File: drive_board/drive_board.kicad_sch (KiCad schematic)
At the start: 7 parts, among them J2 RJ45_LED_Shielded

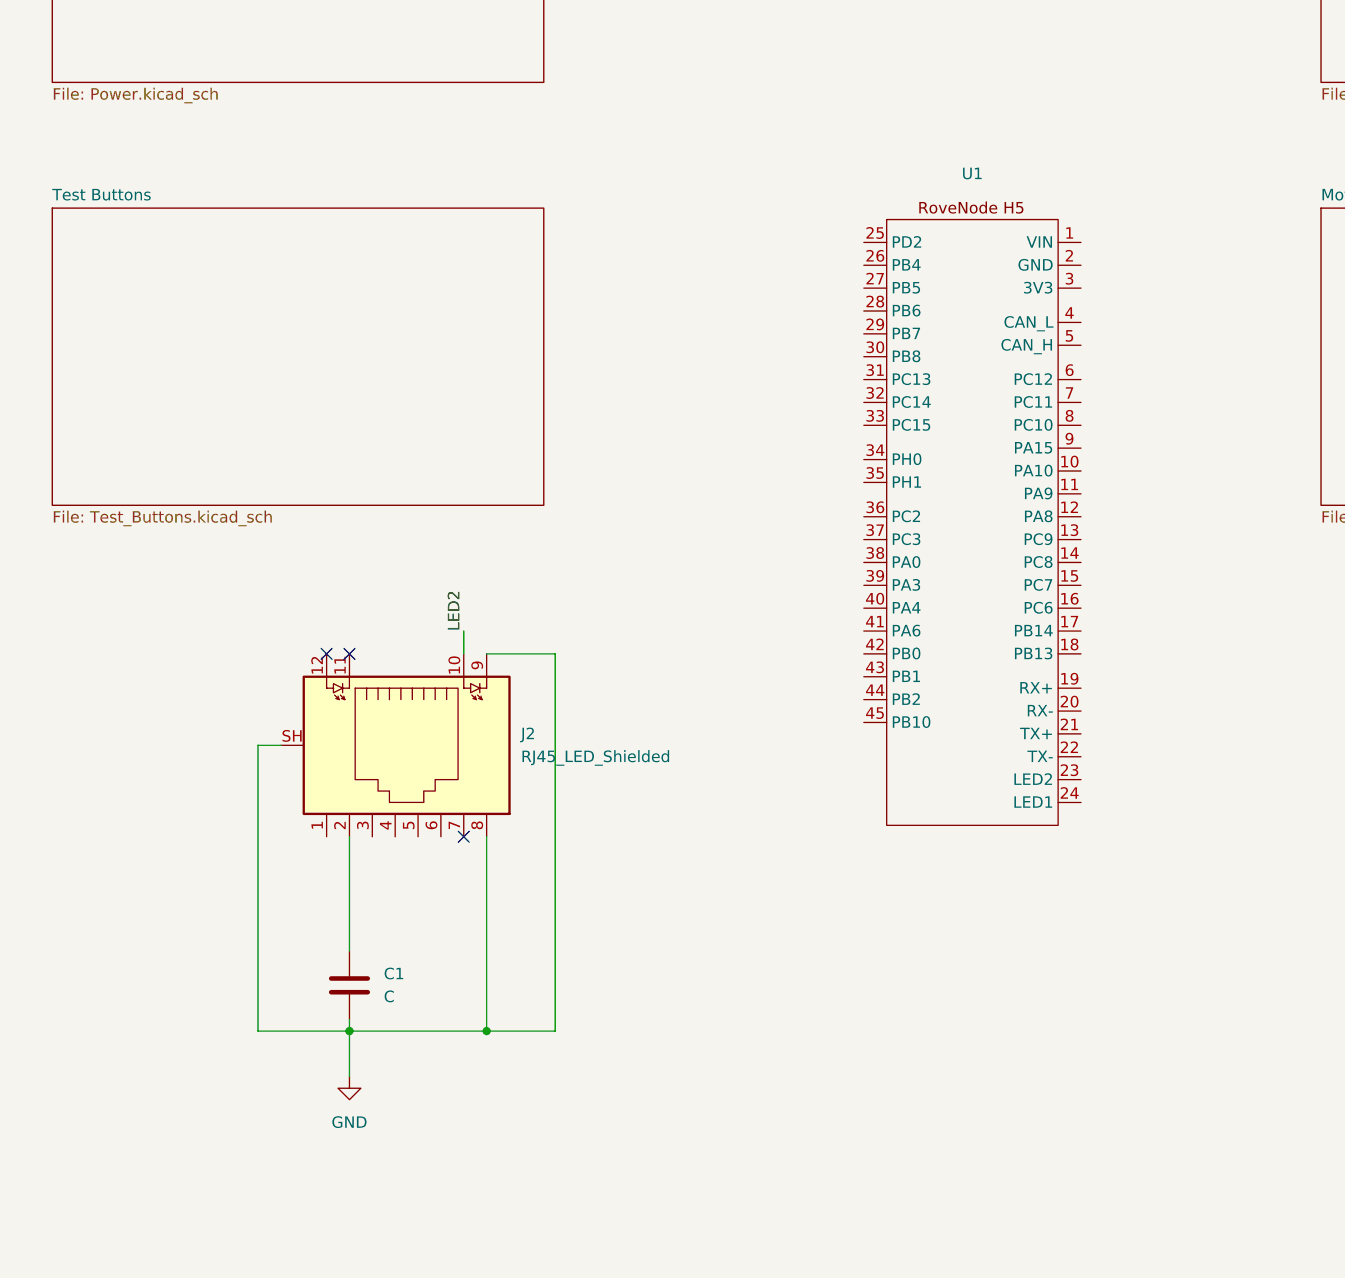
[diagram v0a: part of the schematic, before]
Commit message: New Stuff
- Reverse voltage protection
- D-Pad for test buttons
- Rotary encoder for test buttons
- Finished ethernet circuit
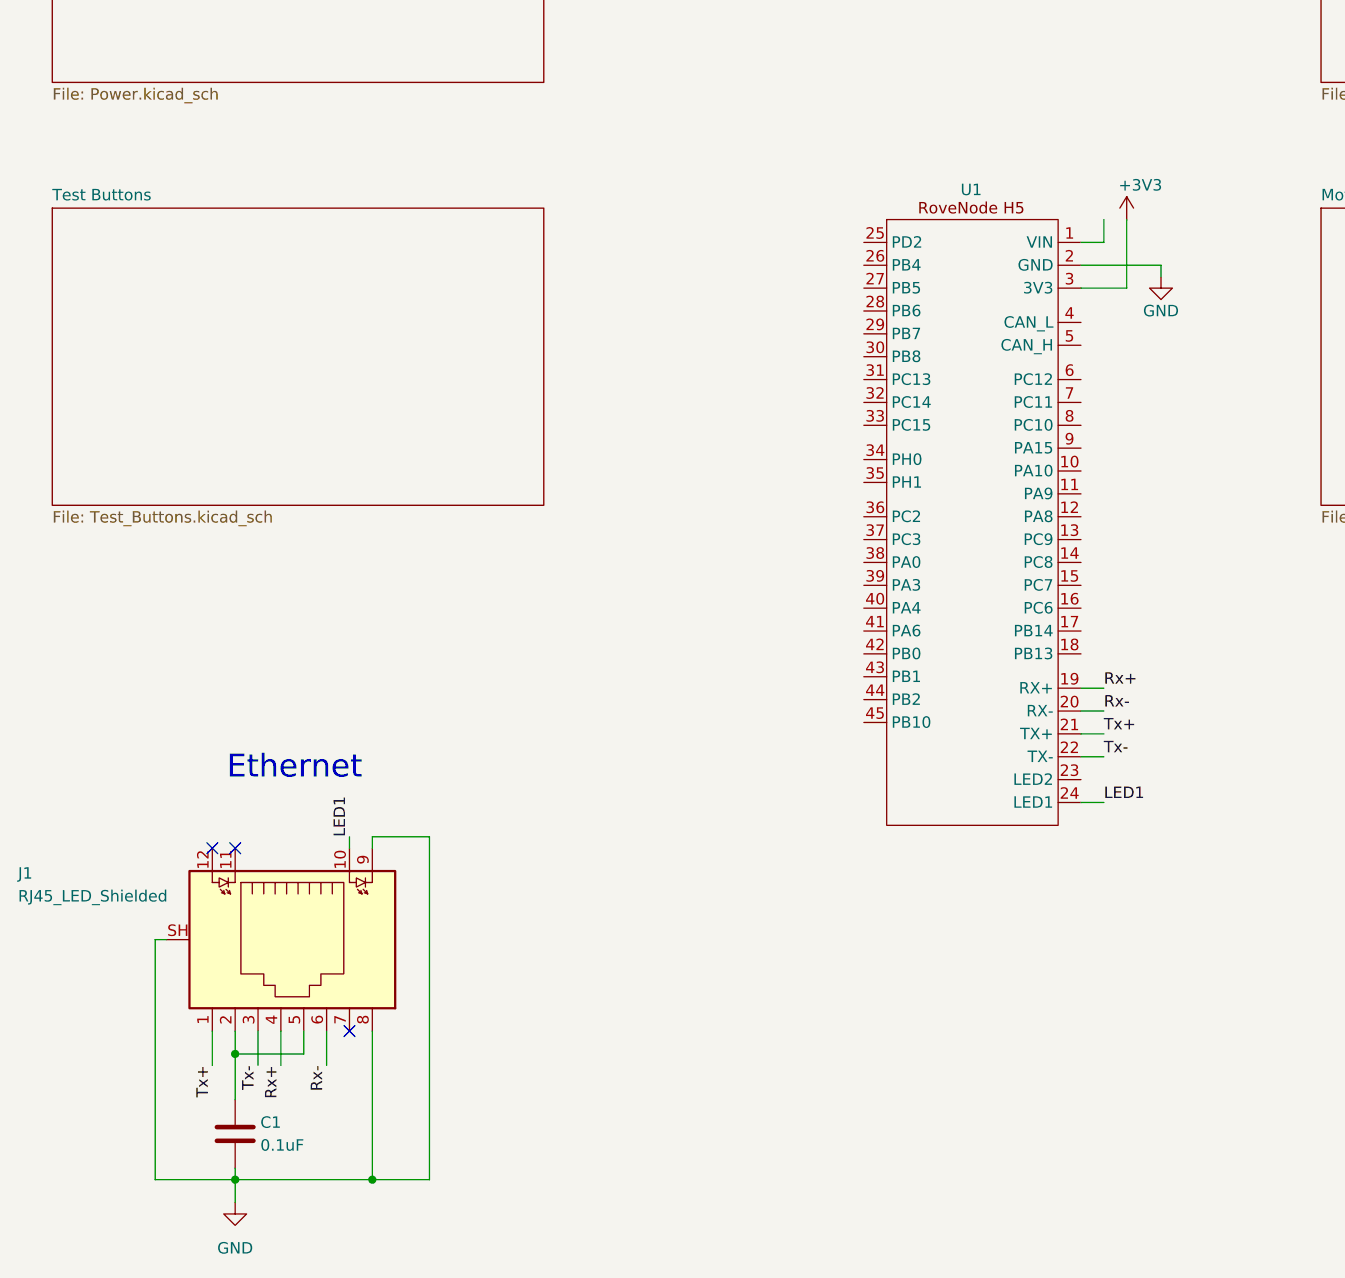
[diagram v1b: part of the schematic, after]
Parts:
- C1: value C -> 0.1uF
- renumbered J2 to J1
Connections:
- net LED2 is gone; now on net LED1: J1.10
- net GND: now also U1.2 (GND)
- net Rx+: now reaches U1.19 (RX+)
- net Rx+: now also J1.4
- net Rx-: now reaches U1.20 (RX-)
- net Rx-: now also J1.6
- net Tx+: now reaches U1.21 (TX+)
- net Tx+: now also J1.1
- net Tx-: now reaches U1.22 (TX-)
- net Tx-: now also J1.3
- net LED1: now reaches U1.24 (LED1)
- net +3V3: now reaches U1.3 (3V3)
- net at C1.1, J1.2: now also J1.5
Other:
- note added: "Ethernet"
- moved on the sheet: C1, J1

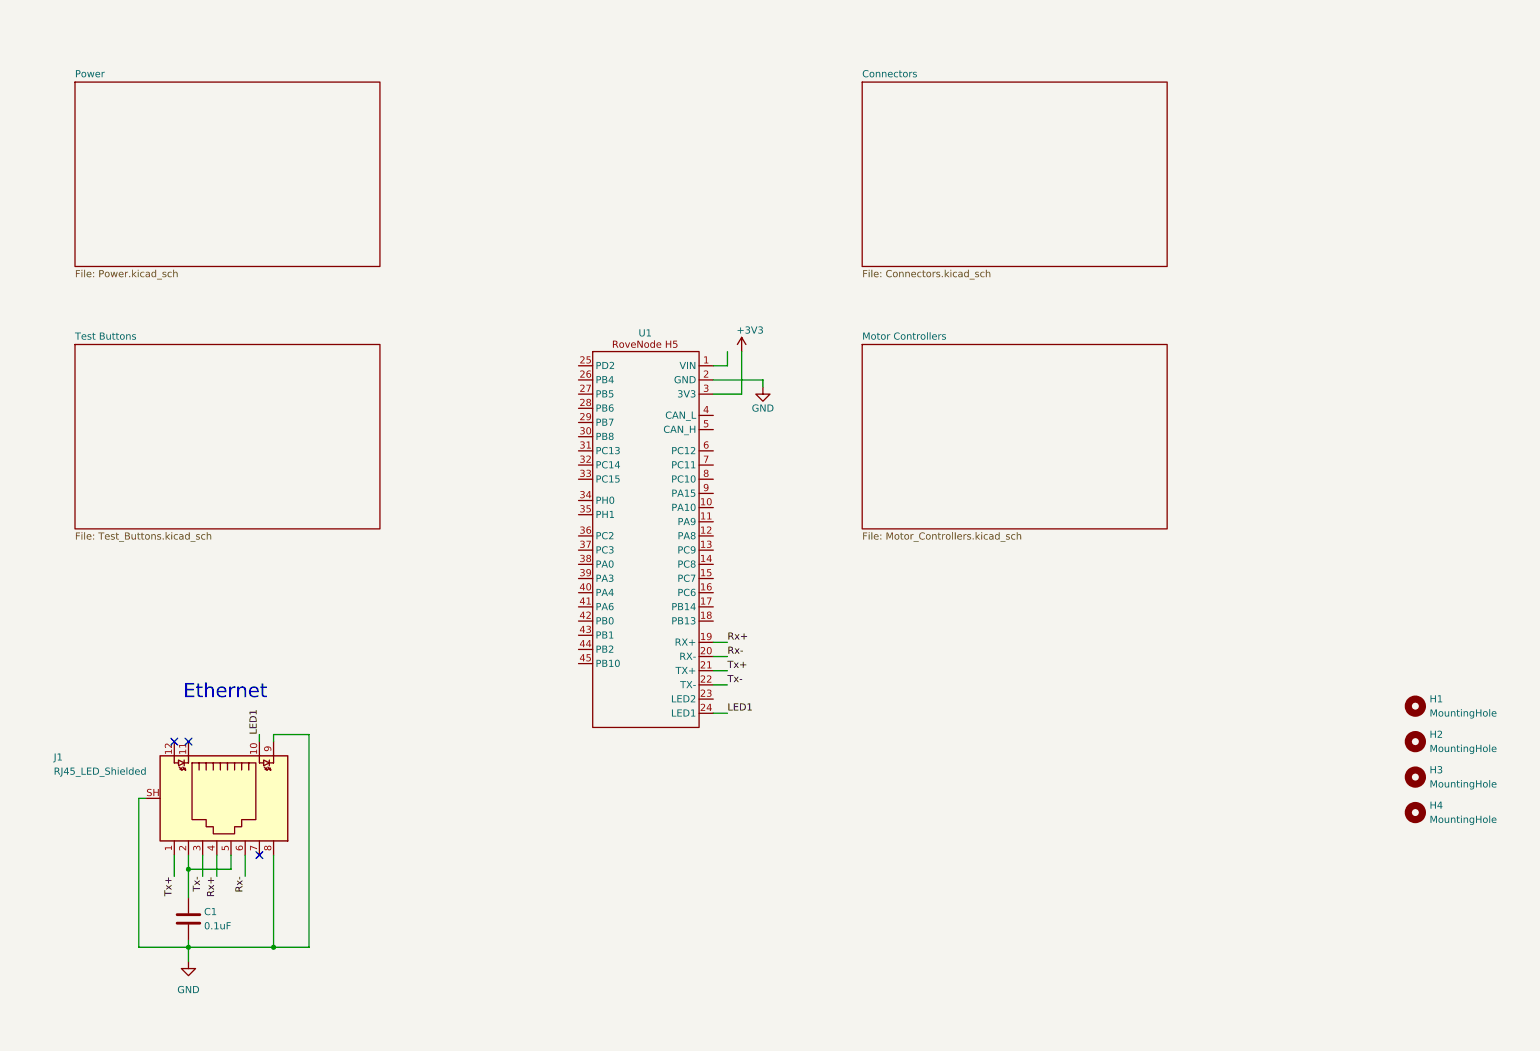
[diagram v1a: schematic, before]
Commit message: More New Stuff
- Assigned pins on RoveNode
- Added some connectors
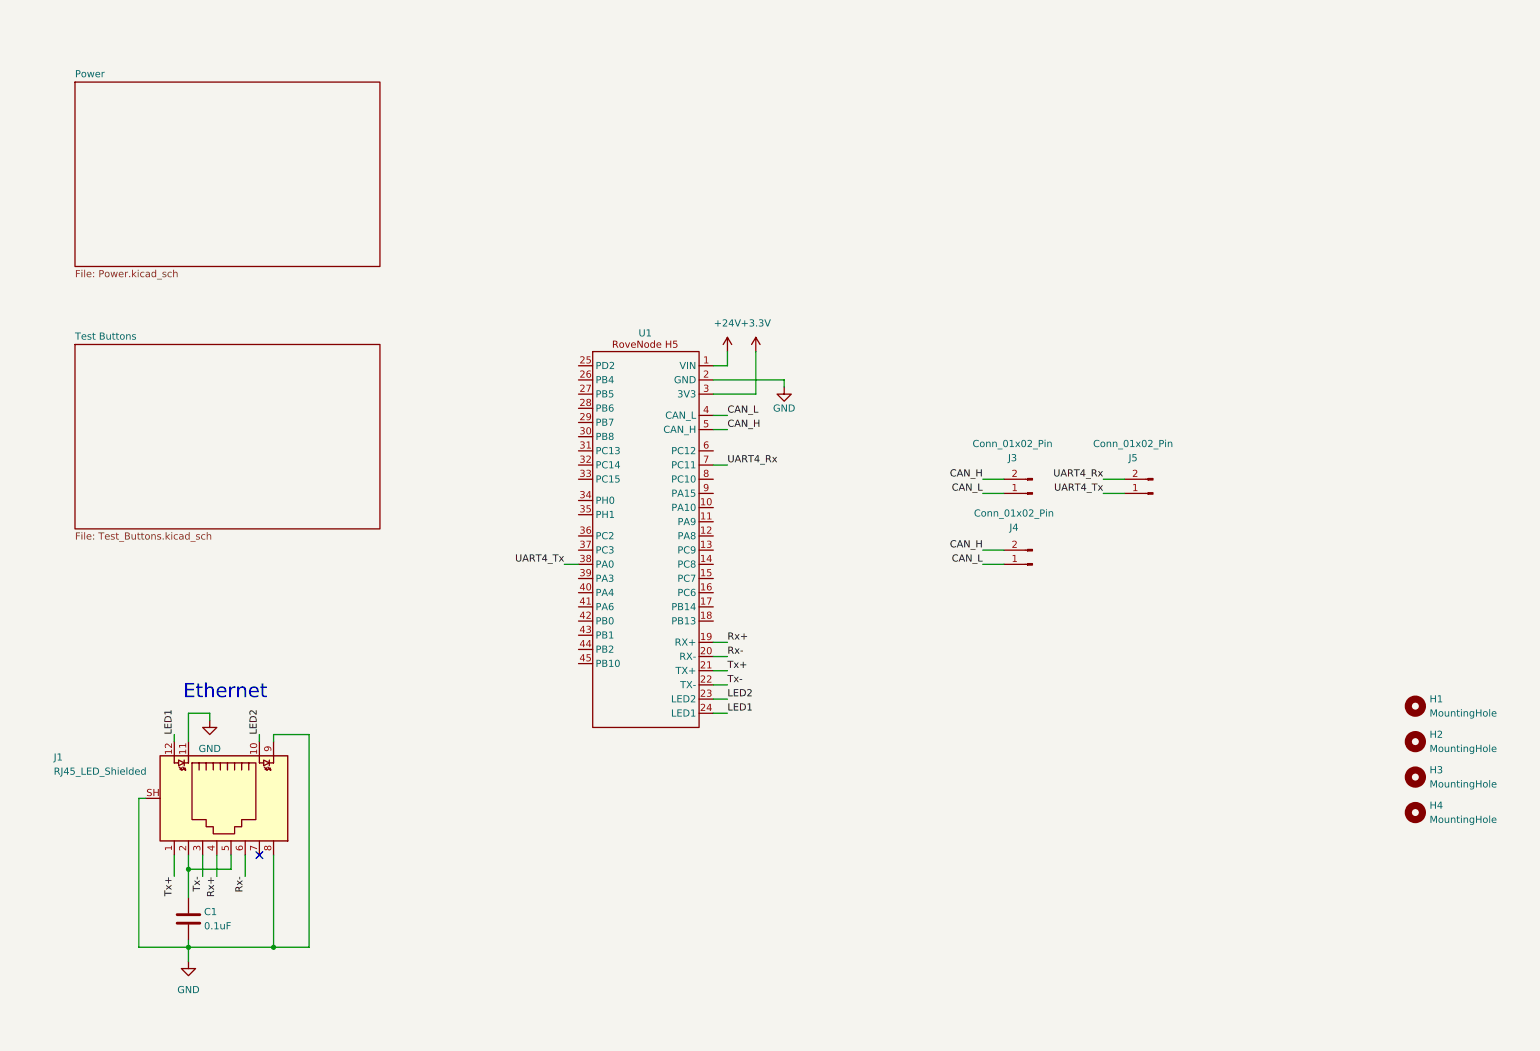
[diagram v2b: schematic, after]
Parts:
- added J3, J4, J5: Conn_01x02_Pin, Package_DFN_QFN:QFN-20-1EP_5x5mm_P0.65mm_EP3.35x3.35mm, symbol Connector:Conn_01x02_Pin
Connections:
- net GND: now also J1.11
- net LED1: now also J1.12; no longer J1.10
- net +24V: now reaches U1.1 (VIN)
- net LED2: now reaches U1.23 (LED2)
- net LED2: now also J1.10
- net UART4_Tx: now reaches U1.38 (PA0)
- net UART4_Tx: now also J5.1 (Pin_1)
- net CAN_L: now reaches U1.4 (CAN_L)
- net CAN_L: now also J3.1 (Pin_1), J4.1 (Pin_1)
- net CAN_H: now reaches U1.5 (CAN_H)
- net CAN_H: now also J3.2 (Pin_2), J4.2 (Pin_2)
- net UART4_Rx: now reaches U1.7 (PC11)
- net UART4_Rx: now also J5.2 (Pin_2)
- net +3V3 renamed +3.3V
- no-connect marks 3 -> 1
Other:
- removed sheet Connectors
- removed sheet Motor Controllers

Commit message: Even More New Stuff
- CAN Transceiver
- Global and hierarchal labels
- How the heck does the rotary encoder work? Lmk when I'm in the office.
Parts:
- added R9: 120, Resistor_SMD:R_0603_1608Metric_Pad0.98x0.95mm_HandSolder, symbol Device:R_US
- added U3: SN65HVD232, Package_SO:SOIC-8_3.9x4.9mm_P1.27mm, symbol Interface_CAN_LIN:SN65HVD232
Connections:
- net GND: now also U3.2 (GND)
- net CAN2_TX: now reaches U1.18 (PB13)
- net CAN2_RX: now reaches U1.27 (PB5)
- net CAN2_RX: now also U3.4 (R)
- net CAN_H renamed CAN_H_1
- net CAN_H_1: no longer J4.2 (Pin_2)
- net CAN_L renamed CAN_L_1
- net CAN_L_1: no longer J4.1 (Pin_1)
- net Rx+ renamed RX+
- net Rx- renamed RX-
- net Tx+ renamed TX+
- net Tx- renamed TX-
- net UART4_Rx renamed UART4_RX
- net UART4_Tx renamed UART4_TX
- new net +3V3: U3.3 (VCC)
- new net CAN1_TX: U3.1 (D)
- new net CAN_H_2: J4.2 (Pin_2), R9.1, U3.7 (CANH)
- new net CAN_L_2: J4.1 (Pin_1), R9.2, U3.6 (CANL)
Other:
- sheet Test Buttons ports: added Back, Forward, Left, RTRY1, RTRY2, RTRY4, Right; removed none
- note added: "CAN Transceiver"
- moved on the sheet: C1, J5
